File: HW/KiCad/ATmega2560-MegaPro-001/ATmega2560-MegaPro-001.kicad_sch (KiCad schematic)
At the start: 51 parts, among them J1 Conn_02x16_Odd_Even, J2 Conn_02x21_Odd_Even, J3 Conn_02x03_Odd_Even, J4 AVR-ISP-6, J5 USB_B_Micro, U1 ATMEGA2560-16AU, U2 CH340G, U3 AMS1117-5.0, U4 AMS1117-3.3, Y1 16 MHz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

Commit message: ATmega2560-MegaPro-001 schema
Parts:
- removed R1: R, Resistor_SMD:R_0603_1608Metric, symbol Device:R
- R10, R11: value R -> 682
- R7, R9: value R -> ---; now not fitted
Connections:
- net +5V: now also C6.1, C7.1, C8.1, J4.2 (VCC)
- net D20: now also J2.31 (Pin_31)
- net D21: now also J2.32 (Pin_32)
- net GND: now also C5.2, C6.2, C7.2, C8.2, J4.6 (GND)
- net Reset: now also J4.5 (~{RST})
- net D22: now reaches J2.33 (Pin_33)
- net D24: now reaches J2.35 (Pin_35)
- net D26: now reaches J2.37 (Pin_37)
- net A15: now reaches U1.82 (PK7(ADC15/PCINT23))
- net A14: now reaches U1.83 (PK6(ADC14/PCINT22))
- net A13: now reaches U1.84 (PK5(ADC13/PCINT21))
- net A12: now reaches U1.85 (PK4(ADC12/PCINT20))
- net A11: now reaches U1.86 (PK3(ADC11/PCINT19))
- net A10: now reaches U1.87 (PK2(ADC10/PCINT18))
- net A9: now reaches U1.88 (PK1(ADC9/PCINT17))
- net A8: now reaches U1.89 (PK0(ADC8/PCINT16))
- net A7: now reaches U1.90 ((ADC7/TDI)PF7)
- net A6: now reaches U1.91 ((ADC6/TDO)PF6)
- net A5: now reaches U1.92 ((ADC5/TMS)PF5)
- net A4: now reaches U1.93 ((ADC4/TCK)PF4)
- net A3: now reaches U1.94 ((ADC3)PF3)
- net A3: now also J1.4 (Pin_4)
- net A2: now reaches U1.95 ((ADC2)PF2)
- net A2: now also J1.3 (Pin_3)
- net A1: now reaches U1.96 ((ADC1)PF1)
- net A1: now also J1.2 (Pin_2)
- net A0: now reaches U1.97 ((ADC0)PF0)
- net A0: now also J1.1 (Pin_1)
- net at U1.98 (AREF): now also C5.1
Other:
- note added: "SCL"
- note added: "SDA"
- moved on the sheet: C13, C14, C5, C6, C7, C8, R15, Y1

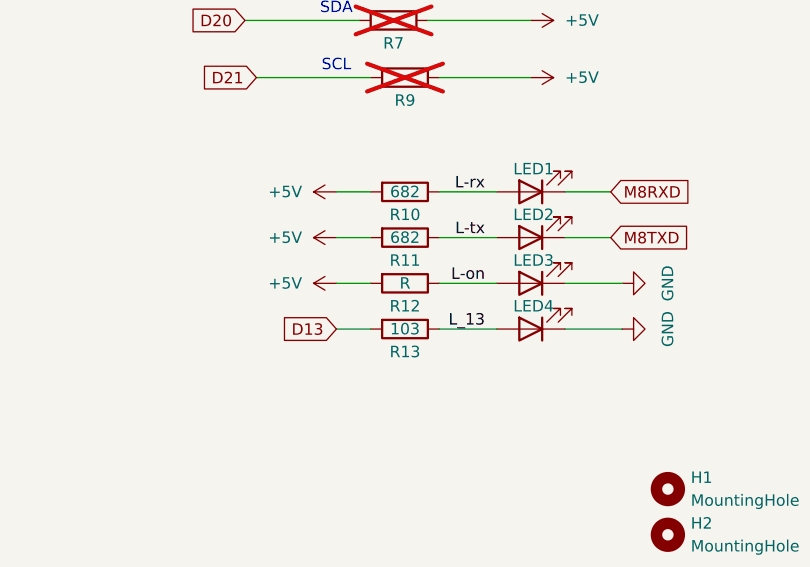
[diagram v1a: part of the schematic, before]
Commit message: +3d models, +Pins.rst, some reorganisation
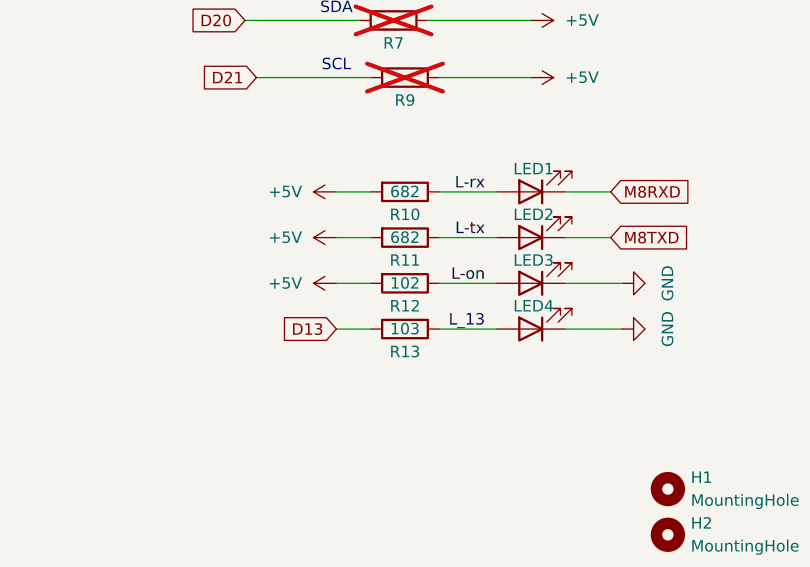
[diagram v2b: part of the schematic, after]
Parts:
- R12: value R -> 102
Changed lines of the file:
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@@
 			)
 		)
-		(property "Value" "R"
+		(property "Value" "102"
 			(at 341.63 96.52 90)
 			(effects
